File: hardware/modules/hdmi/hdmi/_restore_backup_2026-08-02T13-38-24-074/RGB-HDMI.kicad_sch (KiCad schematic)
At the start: 25 parts, among them J1 HDMI_A, U2 TFP410PAP, U4 UCL0524P, U5 UCL0524P, U6 UCL0524P

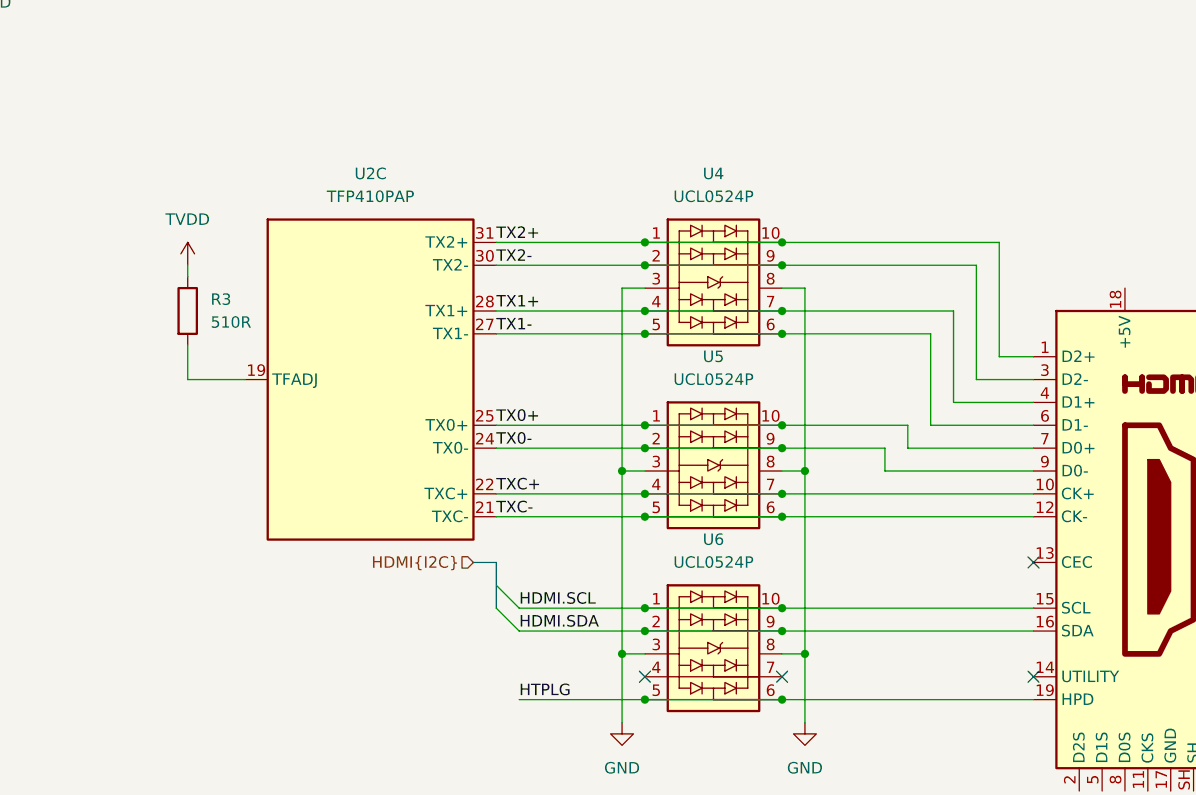
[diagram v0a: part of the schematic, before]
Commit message: Almost finished schematic and started on layout idea's of hdmi module
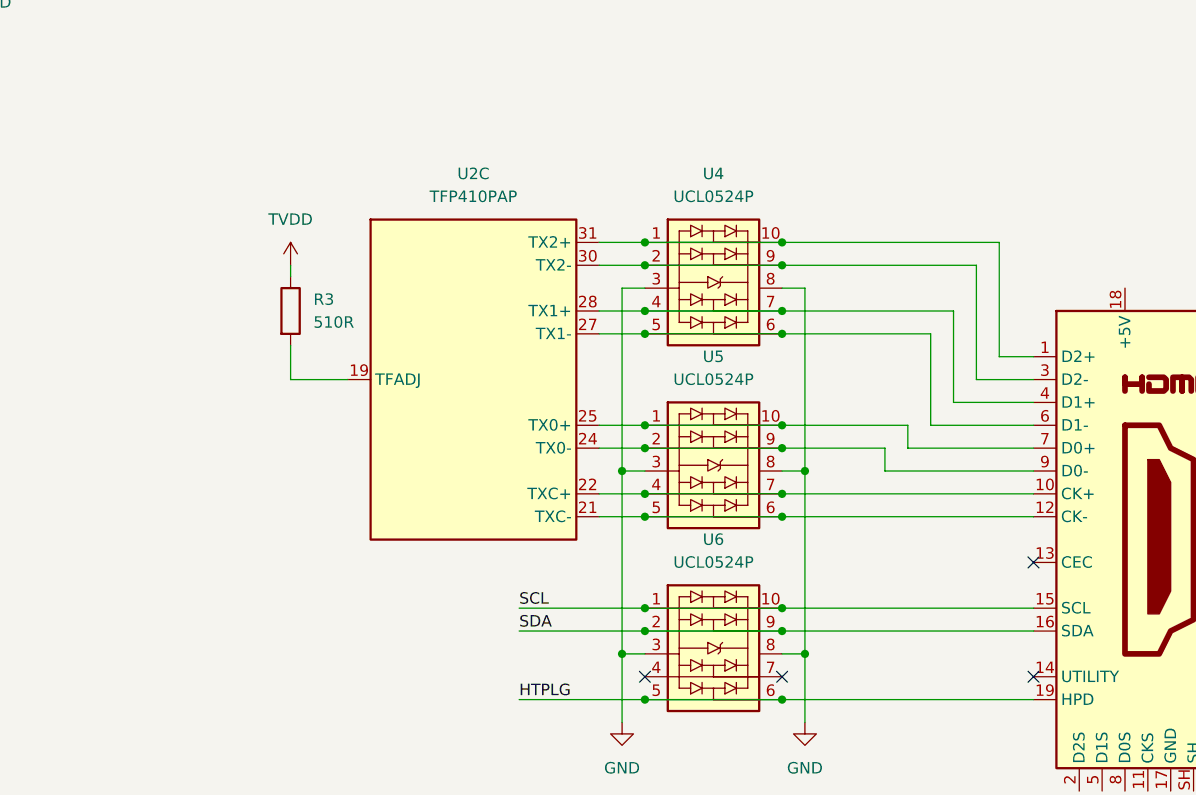
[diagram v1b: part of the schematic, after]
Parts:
- C16, C17, C18, C19, C22, C23, C24, C25, C27, C28, C29, C30: footprint Capacitor_SMD:C_0402_1005Metric -> Capacitor_SMD:C_0603_1608Metric
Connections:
- net HDMI.SCL is gone; now on net SCL: J1.15 (SCL), U6.1, U6.10
- net HDMI.SDA is gone; now on net SDA: J1.16 (SDA), U6.2, U6.9
- net TX0+: no longer names the net of J1.7 (D0+), U2.25 (TX0+), U5.1, U5.10
- net TX0-: no longer names the net of J1.9 (D0-), U2.24 (TX0-), U5.2, U5.9
- net TX1+: no longer names the net of J1.4 (D1+), U2.28 (TX1+), U4.4, U4.7
- net TX1-: no longer names the net of J1.6 (D1-), U2.27 (TX1-), U4.5, U4.6
- net TX2+: no longer names the net of J1.1 (D2+), U2.31 (TX2+), U4.1, U4.10
- net TX2-: no longer names the net of J1.3 (D2-), U2.30 (TX2-), U4.2, U4.9
- net TXC+: no longer names the net of J1.10 (CK+), U2.22 (TXC+), U5.4, U5.7
- net TXC-: no longer names the net of J1.12 (CK-), U2.21 (TXC-), U5.5, U5.6
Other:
- moved on the sheet: R3, U2C
